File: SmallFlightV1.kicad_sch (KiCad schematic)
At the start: 0 parts

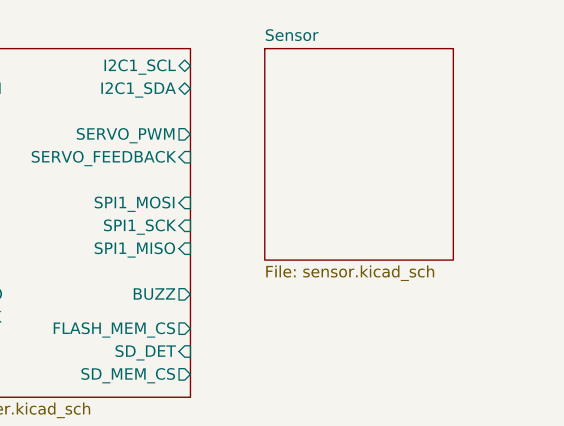
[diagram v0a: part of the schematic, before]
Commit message: wiring the IMU as per its datasheet app circuit. started with power rails
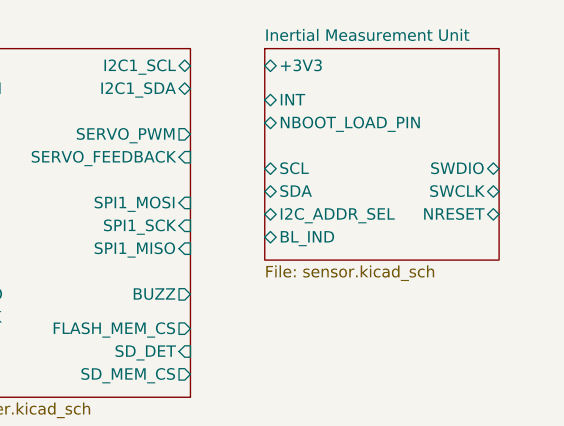
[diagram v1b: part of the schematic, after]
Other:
- sheet Sensor renamed Inertial Measurement Unit
- sheet Inertial Measurement Unit ports: added +3V3, BL_IND, I2C_ADDR_SEL, INT, NBOOT_LOAD_PIN, NRESET, SCL, SDA, SWCLK, SWDIO; removed none
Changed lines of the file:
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@@
 	(sheet
 		(at 170.815 31.115)
-		(size 20.955 23.495)
+		(size 26.035 23.495)
 		(exclude_from_sim no)
 		(in_bom yes)
@@
 			(color 0 0 0 0)
 		)
-		(property "Sheetname" "Sensor"
+		(property "Sheetname" "Inertial Measurement Unit"
 			(at 170.815 30.4034 0)
 			(show_name no)
@@
 			)
 		)
+		(pin "BL_IND" bidirectional
+			(at 170.815 52.07 180)
+			(effects
+				(font
+					(size 1.27 1.27)
+				)
+				(justify left)
+			)
+		)
+		(pin "NRESET" bidirectional
+			(at 196.85 49.53 0)
+			(effects
+				(font
+					(size 1.27 1.27)
+				)
+				(justify right)
+			)
+		)
+		(pin "SWCLK" bidirectional
+			(at 196.85 46.99 0)
+			(effects
+				(font
+					(size 1.27 1.27)
+				)
+				(justify right)
+			)
+		)
+		(pin "SWDIO" bidirectional
+			(at 196.85 44.45 0)
+			(effects
+				(font
+					(size 1.27 1.27)
+				)
+				(justify right)
+			)
+		)
+		(pin "NBOOT_LOAD_PIN" bidirectional
+			(at 170.815 39.37 180)
+			(effects
+				(font
+					(size 1.27 1.27)
+				)
+				(justify left)
+			)
+		)
+		(pin "INT" bidirectional
+			(at 170.815 36.83 180)
+			(effects
+				(font
+					(size 1.27 1.27)
+				)
+				(justify left)
+			)
+		)
+		(pin "SDA" bidirectional
+			(at 170.815 46.99 180)
+			(effects
+				(font
+					(size 1.27 1.27)
+				)
+				(justify left)
+			)
+		)
+		(pin "I2C_ADDR_SEL" bidirectional
+			(at 170.815 49.53 180)
+			(effects
+				(font
+					(size 1.27 1.27)
+				)
+				(justify left)
+			)
+		)
+		(pin "+3V3" bidirectional
+			(at 170.815 33.02 180)
+			(effects
+				(font
+					(size 1.27 1.27)
+				)
+				(justify left)
+			)
+		)
+		(pin "SCL" bidirectional
+			(at 170.815 44.45 180)
+			(effects
+				(font
+					(size 1.27 1.27)
+				)
+				(justify left)
+			)
+		)

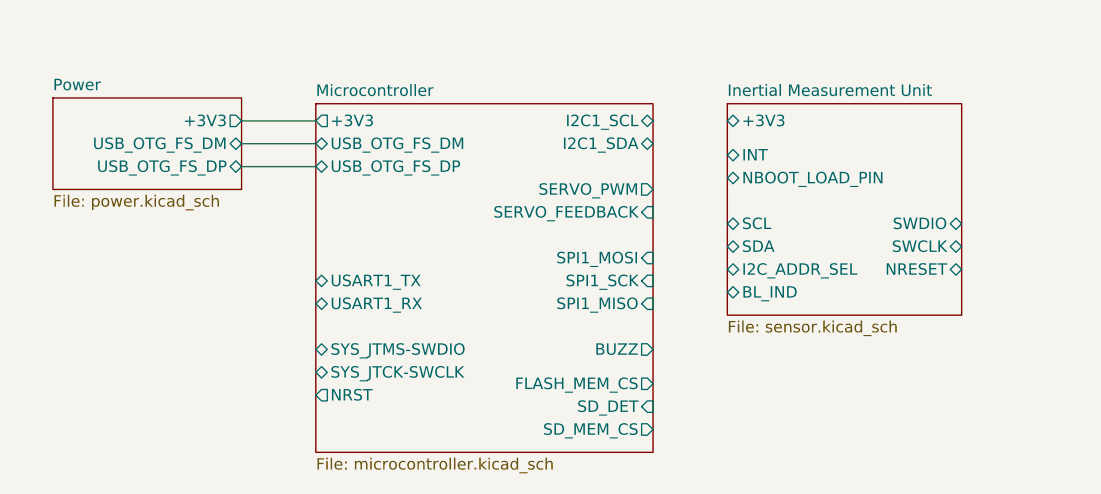
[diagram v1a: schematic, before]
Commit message: IMU wiring
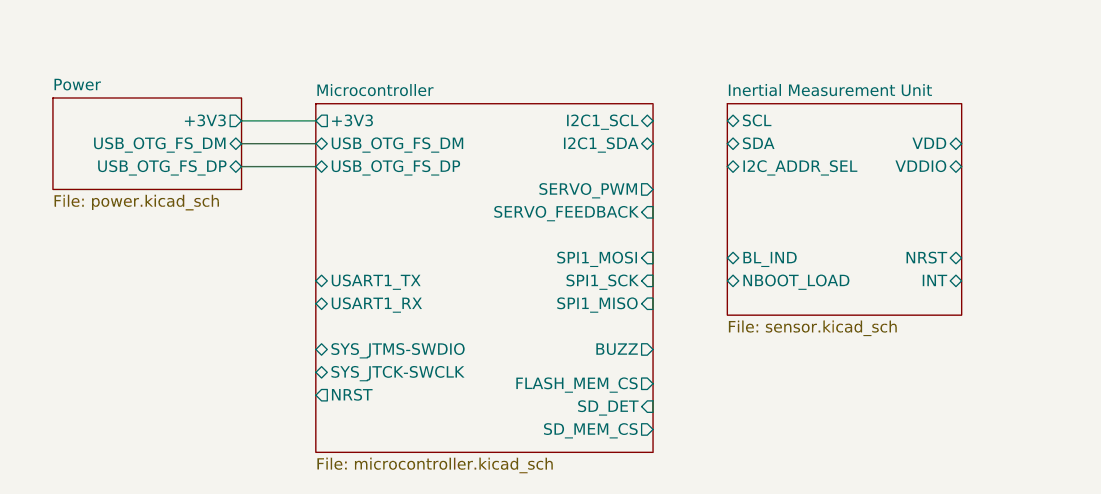
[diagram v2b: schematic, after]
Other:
- sheet Inertial Measurement Unit ports: added NBOOT_LOAD, NRST, SCL , VDD, VDDIO; removed +3V3, NBOOT_LOAD_PIN, NRESET, SCL, SWCLK, SWDIO
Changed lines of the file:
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@@
 		)
 		(pin "BL_IND" bidirectional
-			(at 170.815 52.07 180)
-			(effects
-				(font
-					(size 1.27 1.27)
-				)
-				(justify left)
-			)
-		)
-		(pin "NRESET" bidirectional
-			(at 196.85 49.53 0)
-			(effects
-				(font
-					(size 1.27 1.27)
-				)
-				(justify right)
-			)
-		)
-		(pin "SWCLK" bidirectional
-			(at 196.85 46.99 0)
-			(effects
-				(font
-					(size 1.27 1.27)
-				)
-				(justify right)
-			)
-		)
-		(pin "SWDIO" bidirectional
-			(at 196.85 44.45 0)
-			(effects
-				(font
-					(size 1.27 1.27)
-				)
-				(justify right)
-			)
-		)
-		(pin "NBOOT_LOAD_PIN" bidirectional
-			(at 170.815 39.37 180)
+			(at 170.815 48.26 180)
 			(effects
 				(font
@@
 		)
 		(pin "INT" bidirectional
-			(at 170.815 36.83 180)
+			(at 196.85 50.8 0)
 			(effects
 				(font
 					(size 1.27 1.27)
 				)
-				(justify left)
+				(justify right)
 			)
 		)
 		(pin "SDA" bidirectional
-			(at 170.815 46.99 180)
+			(at 170.815 35.56 180)
 			(effects
 				(font
@@
 		)
 		(pin "I2C_ADDR_SEL" bidirectional
-			(at 170.815 49.53 180)
+			(at 170.815 38.1 180)
 			(effects
 				(font
@@
 			)
 		)
-		(pin "+3V3" bidirectional
+		(pin "VDDIO" bidirectional
+			(at 196.85 38.1 0)
+			(effects
+				(font
+					(size 1.27 1.27)
+				)
+				(justify right)
+			)
+		)
+		(pin "VDD" bidirectional
+			(at 196.85 35.56 0)
+			(effects
+				(font
+					(size 1.27 1.27)
+				)
+				(justify right)
+			)
+		)
+		(pin "NRST" bidirectional
+			(at 196.85 48.26 0)
+			(effects
+				(font
+					(size 1.27 1.27)
+				)
+				(justify right)
+			)
+		)
+		(pin "SCL " bidirectional
 			(at 170.815 33.02 180)
 			(effects
@@
 			)
 		)
-		(pin "SCL" bidirectional
-			(at 170.815 44.45 180)
+		(pin "NBOOT_LOAD" bidirectional
+			(at 170.815 50.8 180)
 			(effects
 				(font

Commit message: barometer schematic
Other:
- added sheet Barometer (barometer.kicad_sch)
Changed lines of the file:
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@@
 	(generator_version "10.0")
 	(paper "A4")
+	(junction
+		(at 120.65 33.02)
+		(diameter 0)
+		(color 0 0 0 0)
+	)
+	(junction
+		(at 200.66 35.56)
+		(diameter 0)
+		(color 0 0 0 0)
+	)
 	(wire
 		(pts
@@
 	(wire
 		(pts
-			(xy 116.84 33.02) (xy 125.095 33.02)
+			(xy 116.84 33.02) (xy 120.65 33.02)
+		)
+		(stroke
+			(width 0)
+			(type default)
+		)
+	)
+	(wire
+		(pts
+			(xy 196.85 38.1) (xy 200.66 38.1)
 		)
 		(stroke
@@
 		(pts
 			(xy 116.84 35.56) (xy 125.095 35.56)
+		)
+		(stroke
+			(width 0)
+			(type default)
+		)
+	)
+	(wire
+		(pts
+			(xy 200.66 35.56) (xy 200.66 21.59)
+		)
+		(stroke
+			(width 0)
+			(type default)
+		)
+	)
+	(wire
+		(pts
+			(xy 200.66 38.1) (xy 200.66 35.56)
+		)
+		(stroke
+			(width 0)
+			(type default)
+		)
+	)
+	(wire
+		(pts
+			(xy 120.65 33.02) (xy 125.095 33.02)
+		)
+		(stroke
+			(width 0)
+			(type default)
+		)
+	)
+	(wire
+		(pts
+			(xy 200.66 21.59) (xy 120.65 21.59)
+		)
+		(stroke
+			(width 0)
+			(type default)
+		)
+	)
+	(wire
+		(pts
+			(xy 196.85 35.56) (xy 200.66 35.56)
+		)
+		(stroke
+			(width 0)
+			(type default)
+		)
+	)
+	(wire
+		(pts
+			(xy 120.65 21.59) (xy 120.65 33.02)
 		)
 		(stroke
@@
 	(sheet
 		(at 170.815 31.115)
-		(size 26.035 23.495)
+		(size 26.035 17.145)
 		(exclude_from_sim no)
 		(in_bom yes)
@@
 		)
 		(property "Sheetfile" "sensor.kicad_sch"
-			(at 170.815 55.1946 0)
+			(at 170.815 48.8446 0)
 			(show_name no)
 			(do_not_autoplace no)
@@
 		)
 		(pin "BL_IND" bidirectional
-			(at 170.815 48.26 180)
+			(at 170.815 43.18 180)
 			(effects
 				(font
@@
 		)
 		(pin "INT" bidirectional
-			(at 196.85 50.8 0)
+			(at 196.85 45.72 0)
 			(effects
 				(font
@@
 		)
 		(pin "NRST" bidirectional
-			(at 196.85 48.26 0)
+			(at 196.85 43.18 0)
 			(effects
 				(font
@@
 		)
 		(pin "NBOOT_LOAD" bidirectional
-			(at 170.815 50.8 180)
+			(at 170.815 45.72 180)
 			(effects
 				(font
@@
 				)
 			)
+		)
+	)
+	(sheet
+		(at 170.815 55.245)
+		(size 26.035 11.43)
+		(exclude_from_sim no)
+		(in_bom yes)
+		(on_board yes)
+		(dnp no)
+		(fields_autoplaced yes)
+		(stroke
+			(width 0.1524)
+			(type solid)
+		)
+		(fill
+			(color 0 0 0 0)
+		)
+		(property "Sheetname" "Barometer"
+			(at 170.815 54.5334 0)
+			(show_name no)
+			(do_not_autoplace no)
+			(effects
+				(font
+					(size 1.27 1.27)
+				)
+				(justify left bottom)
+			)
+		)
+		(property "Sheetfile" "barometer.kicad_sch"
+			(at 170.815 67.2596 0)
+			(show_name no)
+			(do_not_autoplace no)
+			(effects
+				(font
+					(size 1.27 1.27)
+				)
+				(justify left top)
+			)
+		)
+		(pin "VDDIO" bidirectional
+			(at 196.85 59.69 0)
+			(effects
+				(font
+					(size 1.27 1.27)
+				)
+				(justify right)
+			)
+		)
+		(pin "VDD" bidirectional
+			(at 196.85 62.23 0)
+			(effects
+				(font
+					(size 1.27 1.27)
+				)
+				(justify right)
+			)
+		)
+		(pin "SCL" bidirectional
+			(at 170.815 59.69 180)
+			(effects
+				(font
+					(size 1.27 1.27)
+				)
+				(justify left)
+			)
+		)
+		(pin "SDA" bidirectional
+			(at 170.815 62.23 180)
+			(effects
+				(font
+					(size 1.27 1.27)
+				)
+				(justify left)
+			)
+		)
+		(instances
+			(project "SmallFlightV1"
+				(path "/5a8b04a1-a6d6-48bd-ac5f-d4986cb92d03"
+					(page "5")
+				)
+			)

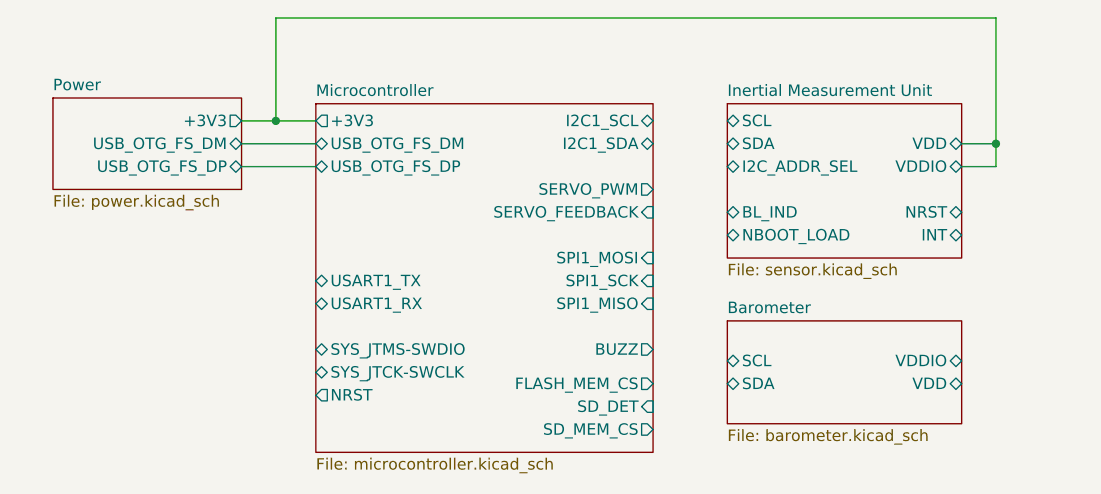
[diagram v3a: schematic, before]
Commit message: update README. update imu to select address, add notte
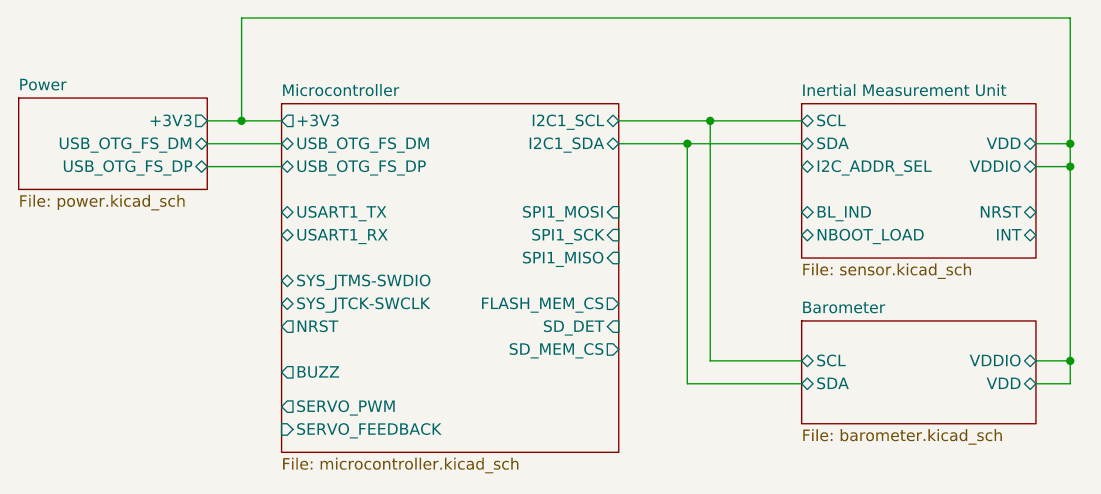
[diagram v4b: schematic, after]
